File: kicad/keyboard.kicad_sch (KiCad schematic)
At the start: 20 parts, among them J1 Conn_01x11_Female, J2 Conn_01x03_Male, SW1 SW_Push, U1 Arduino_pro_Micro

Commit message: TMP: fixing RES and RST
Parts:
- U1: symbol Keyboard:Arduino_pro_Micro -> keyboard:Arduino_Pro_Micro
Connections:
- net GND: now also J1.1 (Pin_1); no longer J1.2 (Pin_2)
- net RAW: now also J1.2 (Pin_2); no longer J1.1 (Pin_1)
- net ~{RES}: now reaches U1.5 (2)
- net ~{RES}: now also J1.5 (Pin_5)
- net RST renamed ~{RST}
- net ~{RST}: no longer J1.5 (Pin_5)
- no-connect marks 9 -> 8
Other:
- sheet left_hand ports: added none; removed RST
- sheet right_hand ports: added none; removed RST
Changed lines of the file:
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@@
   (no_connect (at 167.64 50.8))
   (no_connect (at 167.64 53.34))
-  (no_connect (at 167.64 60.96))
   (wire (pts (xy 167.64 58.42) (xy 165.1 58.42))
     (stroke (width 0) (type default) (color 0 0 0 0))
@@
     (stroke (width 0) (type default) (color 0 0 0 0))
   )
+  (wire (pts (xy 140.97 41.91) (xy 140.97 35.56))
+    (stroke (width 0) (type default) (color 0 0 0 0))
+  )
   (wire (pts (xy 49.53 74.93) (xy 54.61 74.93))
     (stroke (width 0) (type default) (color 0 0 0 0))
   )
-  (wire (pts (xy 143.51 41.91) (xy 143.51 35.56))
-    (stroke (width 0) (type default) (color 0 0 0 0))
-  )
   (wire (pts (xy 104.14 74.93) (xy 109.22 74.93))
     (stroke (width 0) (type default) (color 0 0 0 0))
@@
     (stroke (width 0) (type default) (color 0 0 0 0))
   )
+  (global_label "RAW" (shape bidirectional) (at 143.51 35.56 270) (fields_autoplaced)
+    (effects (font (size 1.27 1.27)) (justify right))
+    (property "Intersheet References" "${INTERSHEET_REFS}" (id 0) (at 143.5894 41.7831 90)
+      (effects (font (size 1.27 1.27)) (justify right) hide)
+    )
+  )
+  (global_label "~{RES}" (shape output) (at 167.64 60.96 180) (fields_autoplaced)
+    (effects (font (size 1.27 1.27)) (justify right))
+    (property "Intersheet References" "${INTERSHEET_REFS}" (id 0) (at 161.5983 60.8806 0)
+      (effects (font (size 1.27 1.27)) (justify right) hide)
+    )
+  )
   (global_label "ROW3" (shape output) (at 189.23 76.2 0) (fields_autoplaced)
     (effects (font (size 1.27 1.27)) (justify left))
@@
     )
   )
-  (global_label "RST" (shape output) (at 189.23 55.88 0) (fields_autoplaced)
+  (global_label "~{RST}" (shape output) (at 189.23 55.88 0) (fields_autoplaced)
     (effects (font (size 1.27 1.27)) (justify left))
     (property "Intersheet References" "${INTERSHEET_REFS}" (id 0) (at 195.0902 55.8006 0)
@@
     )
   )
-  (global_label "RST" (shape output) (at 121.92 97.79 90) (fields_autoplaced)
-    (effects (font (size 1.27 1.27)) (justify left))
-    (property "Intersheet References" "${INTERSHEET_REFS}" (id 0) (at 121.8406 91.9298 90)
-      (effects (font (size 1.27 1.27)) (justify left) hide)
-    )
-  )
   (global_label "SPI_DATA" (shape output) (at 148.59 35.56 270) (fields_autoplaced)
     (effects (font (size 1.27 1.27)) (justify right))
@@
     )
   )
-  (global_label "RAW" (shape bidirectional) (at 140.97 35.56 270) (fields_autoplaced)
-    (effects (font (size 1.27 1.27)) (justify right))
-    (property "Intersheet References" "${INTERSHEET_REFS}" (id 0) (at 141.0494 41.7831 90)
-      (effects (font (size 1.27 1.27)) (justify right) hide)
-    )
-  )
   (global_label "Vin" (shape input) (at 196.85 99.06 0) (fields_autoplaced)
     (effects (font (size 1.27 1.27)) (justify left))
@@
     )
   )
-  (global_label "RST" (shape input) (at 224.79 55.88 0) (fields_autoplaced)
+  (global_label "~{RST}" (shape input) (at 224.79 55.88 0) (fields_autoplaced)
     (effects (font (size 1.27 1.27)) (justify left))
     (property "Intersheet References" "${INTERSHEET_REFS}" (id 0) (at 230.6502 55.8006 0)
@@
     )
   )
-  (global_label "RST" (shape output) (at 74.93 97.79 90) (fields_autoplaced)
-    (effects (font (size 1.27 1.27)) (justify left))
-    (property "Intersheet References" "${INTERSHEET_REFS}" (id 0) (at 74.8506 91.9298 90)
-      (effects (font (size 1.27 1.27)) (justify left) hide)
-    )
-  )
   (global_label "RAW" (shape output) (at 185.42 96.52 0) (fields_autoplaced)
     (effects (font (size 1.27 1.27)) (justify left))
@@
     )
   )
-  (global_label "RST" (shape output) (at 151.13 35.56 270) (fields_autoplaced)
-    (effects (font (size 1.27 1.27)) (justify right))
-    (property "Intersheet References" "${INTERSHEET_REFS}" (id 0) (at 151.0506 41.4202 90)
+  (global_label "~{RES}" (shape output) (at 151.13 35.56 270) (fields_autoplaced)
+    (effects (font (size 1.27 1.27)) (justify right))
+    (property "Intersheet References" "${INTERSHEET_REFS}" (id 0) (at 151.0506 41.6017 90)
       (effects (font (size 1.27 1.27)) (justify right) hide)
     )
@@
     (pin "2")
   )
-  (symbol (lib_id "Keyboard:Arduino_pro_Micro") (at 179.07 64.77 0) (unit 1)
-    (in_bom yes) (on_board yes) (fields_autoplaced)
-    (property "Reference" "U1" (id 0) (at 179.07 45.72 0))
-    (property "Value" "Arduino_pro_Micro" (id 1) (at 179.07 81.28 0))
-    (property "Footprint" "Package_DIP:DIP-24_W15.24mm" (id 2) (at 179.07 46.99 0)
-      (effects (font (size 1.27 1.27)) hide)
-    )
-    (property "Datasheet" "" (id 3) (at 179.07 46.99 0)
+  (symbol (lib_id "keyboard:Arduino_Pro_Micro") (at 167.64 50.8 0) (unit 1)
+    (in_bom yes) (on_board yes) (fields_autoplaced)
+    (property "Reference" "U1" (id 0) (at 167.64 31.75 0))
+    (property "Value" "Arduino_pro_Micro" (id 1) (at 167.64 67.31 0))
+    (property "Footprint" "Package_DIP:DIP-24_W15.24mm" (id 2) (at 177.8 46.99 0)
+      (effects (font (size 1.27 1.27)) hide)
+    )
+    (property "Datasheet" "" (id 3) (at 177.8 46.99 0)
       (effects (font (size 1.27 1.27)) hide)
     )
@@
     (pin "1")
   )
+  (symbol (lib_id "power:GND") (at 140.97 41.91 0) (unit 1)
+    (in_bom yes) (on_board yes) (fields_autoplaced)
+    (property "Reference" "#PWR0114" (id 0) (at 140.97 48.26 0)
+      (effects (font (size 1.27 1.27)) hide)
+    )
+    (property "Value" "GND" (id 1) (at 140.97 45.72 0))
+    (property "Footprint" "" (id 2) (at 140.97 41.91 0)
+      (effects (font (size 1.27 1.27)) hide)
+    )
+    (property "Datasheet" "" (id 3) (at 140.97 41.91 0)
+      (effects (font (size 1.27 1.27)) hide)
+    )
+    (pin "1")
+  )
   (symbol (lib_id "Device:R_US") (at 49.53 71.12 0) (unit 1)
     (in_bom yes) (on_board yes)
@@
     )
     (property "Datasheet" "" (id 3) (at 140.97 74.93 0)
-      (effects (font (size 1.27 1.27)) hide)
-    )
-    (pin "1")
-  )
-  (symbol (lib_id "power:GND") (at 143.51 41.91 0) (unit 1)
-    (in_bom yes) (on_board yes) (fields_autoplaced)
-    (property "Reference" "#PWR01" (id 0) (at 143.51 48.26 0)
-      (effects (font (size 1.27 1.27)) hide)
-    )
-    (property "Value" "GND" (id 1) (at 143.51 45.72 0))
-    (property "Footprint" "" (id 2) (at 143.51 41.91 0)
-      (effects (font (size 1.27 1.27)) hide)
-    )
-    (property "Datasheet" "" (id 3) (at 143.51 41.91 0)
       (effects (font (size 1.27 1.27)) hide)
     )
@@
       (effects (font (size 1.27 1.27)) (justify left))
     )
-    (pin "RST" input (at 121.92 97.79 90)
-      (effects (font (size 1.27 1.27)) (justify right))
-    )
   )
   (sheet (at 62.23 97.79) (size 24.13 13.97)
@@
       (effects (font (size 1.27 1.27)) (justify left))
     )
-    (pin "RST" input (at 74.93 97.79 90)
-      (effects (font (size 1.27 1.27)) (justify right))
-    )
     (pin "ROW1" output (at 86.36 100.33 0)
       (effects (font (size 1.27 1.27)) (justify right))
@@
       (reference "#FLG0102") (unit 1) (value "PWR_FLAG") (footprint "")
     )
-    (path "/bde2327a-a676-461a-91db-75b5a10a64ab"
-      (reference "#PWR01") (unit 1) (value "GND") (footprint "")
-    )
     (path "/474dcb84-dbbe-4064-ab56-e9e164dbe8ae"
       (reference "#PWR0101") (unit 1) (value "GND") (footprint "")
@@
       (reference "#PWR0113") (unit 1) (value "GND") (footprint "")
     )
+    (path "/5300e48f-023c-4382-8a67-63e08d805a1c"
+      (reference "#PWR0114") (unit 1) (value "GND") (footprint "")
+    )
     (path "/44d7977b-848d-467d-9f10-b0bead1499b4"

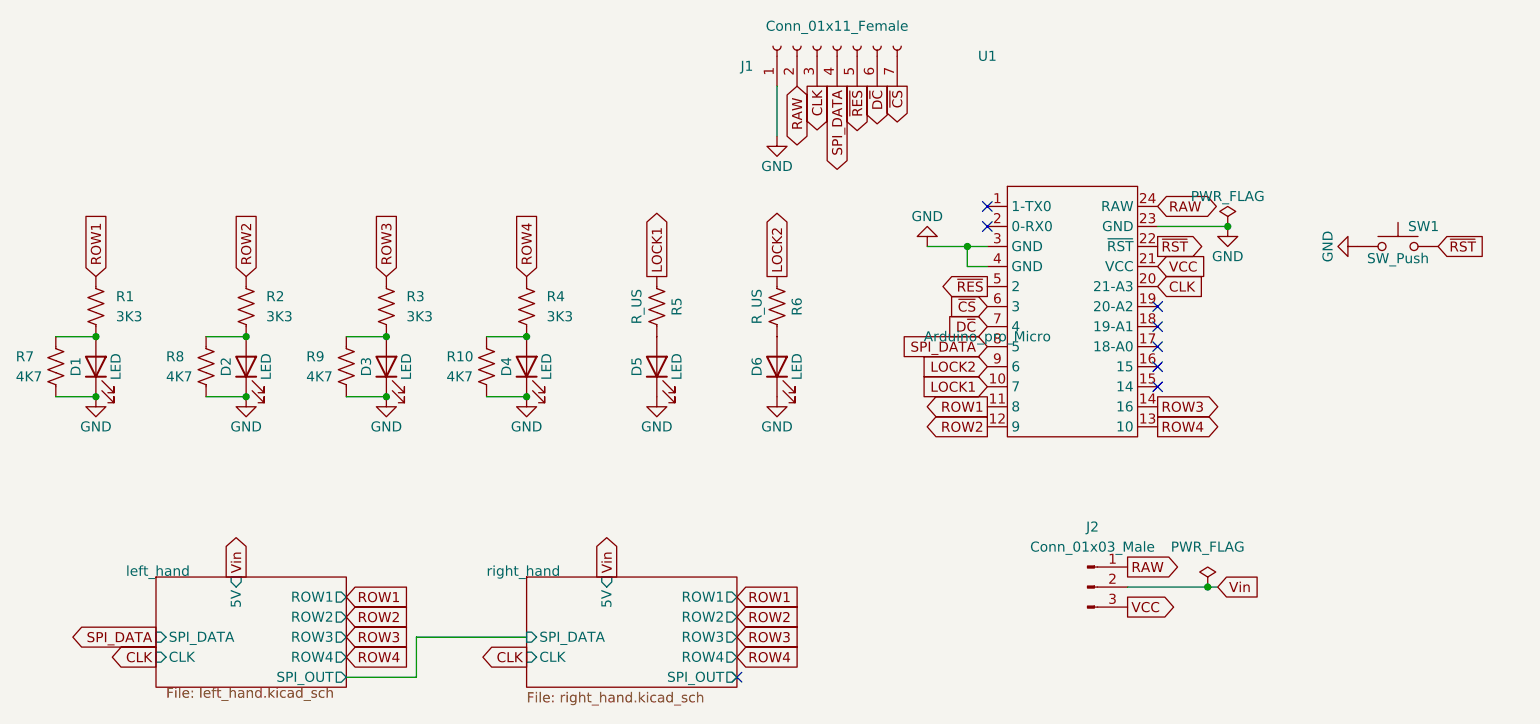
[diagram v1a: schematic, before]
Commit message: TMP: remove unused stuff
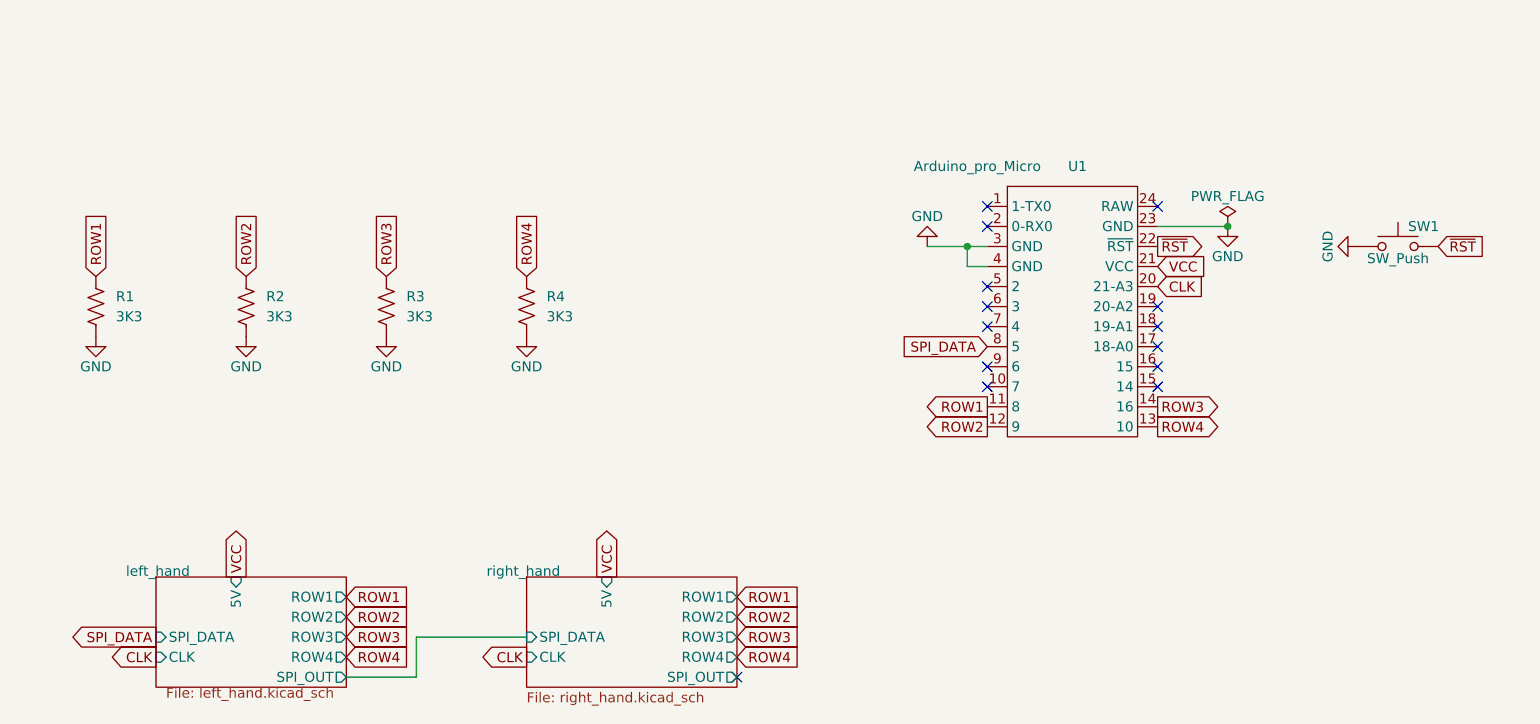
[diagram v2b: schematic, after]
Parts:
- removed D1, D2, D3, D4, D5, D6: LED, Keyboard:LED_D3.0mm, symbol Device:LED
- removed J1: Conn_01x11_Female, Keyboard:PinHeader_01x07, symbol Connector:Conn_01x07_Female
- removed J2: Conn_01x03_Male, Keyboard:PinHeader_01x03, symbol Connector:Conn_01x03_Male
- removed R10, R7, R8, R9: 4K7, Resistor_THT:R_Axial_DIN0207_L6.3mm_D2.5mm_P7.62mm_Horizontal, symbol Device:R_US
- removed R5, R6: R_US, Resistor_THT:R_Axial_DIN0207_L6.3mm_D2.5mm_P7.62mm_Horizontal, symbol Device:R_US
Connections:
- net GND: now also R1.2, R2.2, R3.2, R4.2
- net D~{C}: no longer names the net of U1.7 (4)
- net LOCK1: no longer names the net of U1.10 (7)
- net LOCK2: no longer names the net of U1.9 (6)
- net RAW: no longer names the net of U1.24 (RAW)
- net ~{CS}: no longer names the net of U1.6 (3)
- net ~{RES}: no longer names the net of U1.5 (2)
- no-connect marks 8 -> 14
